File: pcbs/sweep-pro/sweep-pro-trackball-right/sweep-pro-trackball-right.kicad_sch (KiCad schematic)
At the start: 13 parts, among them J10 NFC Antenna, J3 Conn_01x07, J4 Conn_01x07, J5 Conn_01x02, J6 Conn_01x07, J7 Conn_01x03, J8 Conn_01x03, J9 Conn_Display_general

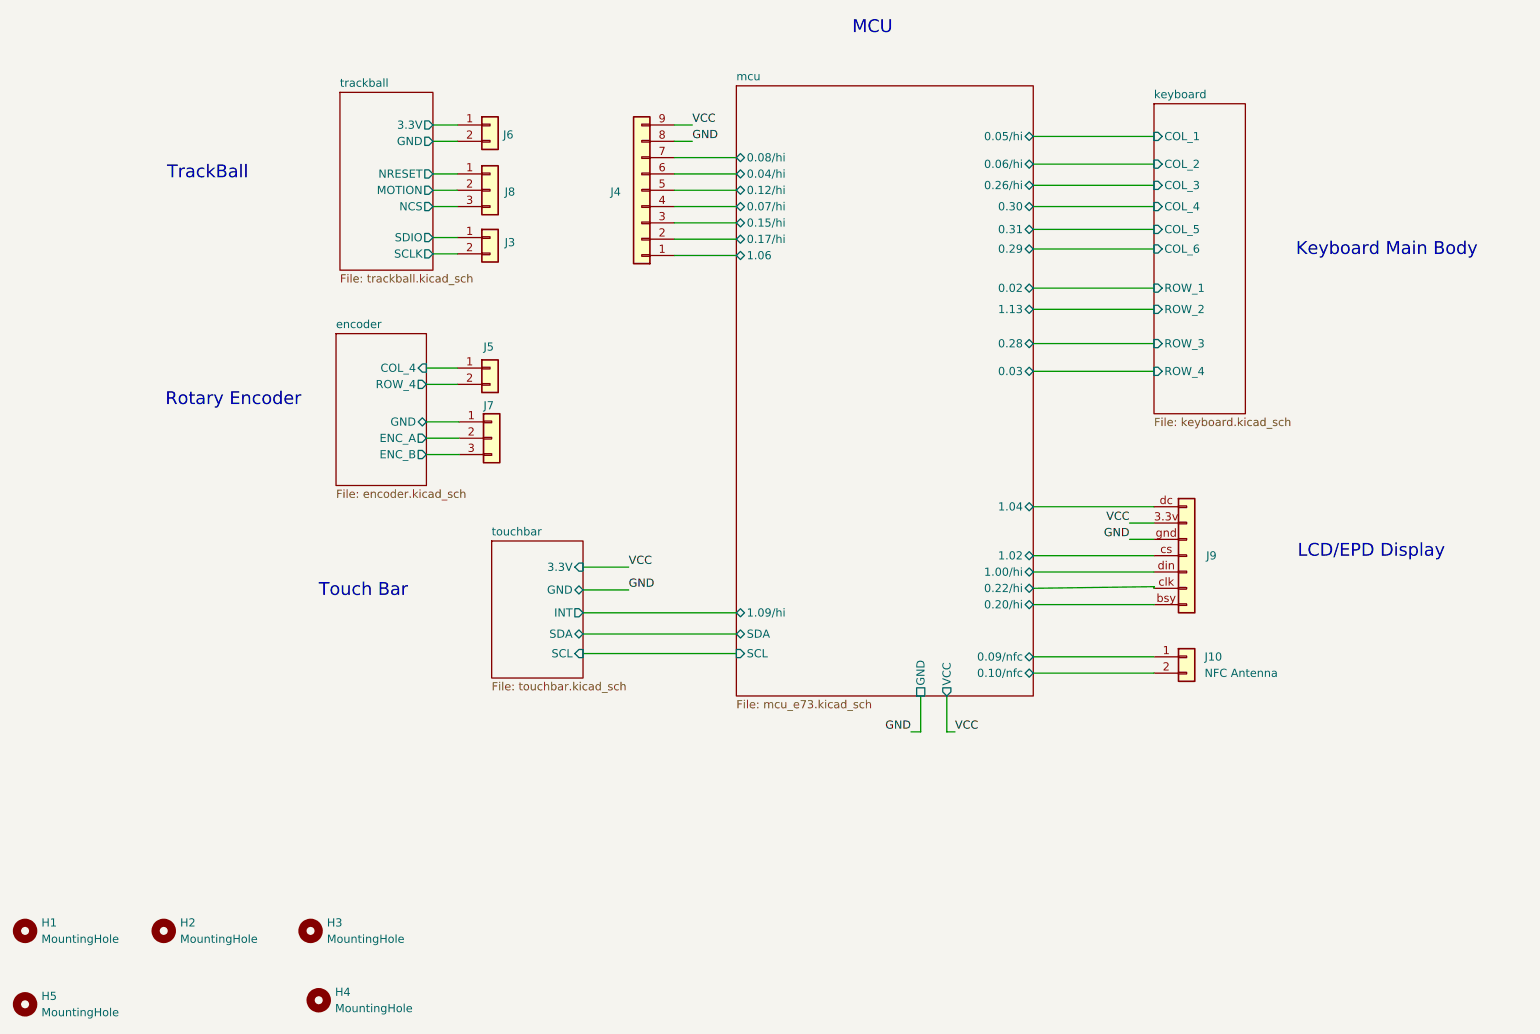
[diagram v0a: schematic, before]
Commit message: init version with integrated trackball in thumb position
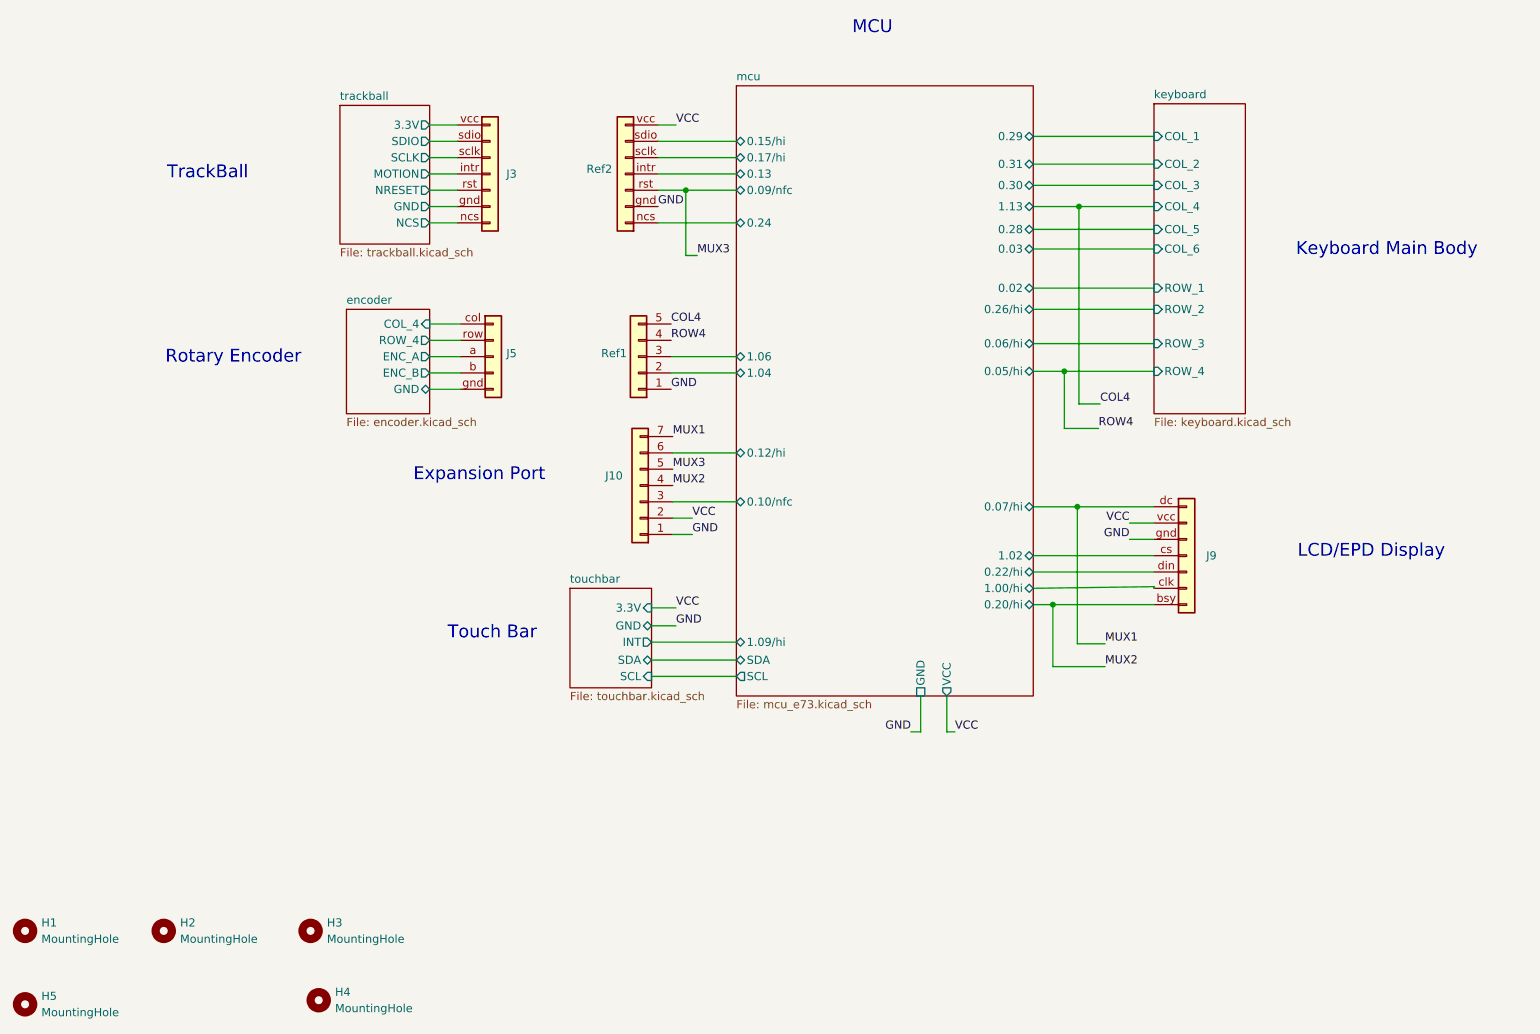
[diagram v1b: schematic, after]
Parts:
- removed J10: NFC Antenna, symbol Connector_Generic:Conn_01x02
- removed J3, J6: Conn_01x07, symbol Connector_Generic:Conn_01x02
- removed J7, J8: Conn_01x03, symbol Connector_Generic:Conn_01x03
- added J10: Conn_01x07, mylib:Magnetic-PogoPin-1x07-Male, symbol Connector_Generic:Conn_01x07
- added J3: Conn_01x07, mylib:PMW3610-Ref-Male, symbol Connector_Generic:Conn_01x07
- added Ref1: Conn_01x05, mylib:Panasonic_EVQWGD001_Ref, symbol Connector_Generic:Conn_01x05
- J5: value Conn_01x02 -> Conn_01x05; footprint (none) -> mylib:Panasonic_EVQWGD001_Ref_Male; symbol Connector_Generic:Conn_01x02 -> Connector_Generic:Conn_01x05; now left out of the parts list
- J9: footprint mylib:Conn_LCD -> mylib:Conn_Display_MountHole
- Ref2: renamed from J4; value Conn_01x07 -> Conn_1x07; footprint (none) -> mylib:PMW3610-Ref; symbol Connector_Generic:Conn_01x09 -> Connector_Generic:Conn_01x07; now left out of the parts list
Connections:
- net GND: now also Ref2.gnd, J10.1 (Pin_1), Ref1.1 (Pin_1); no longer Ref2.8 (Pin_8)
- net VCC: now also J9.vcc, Ref2.vcc, J10.2 (Pin_2); no longer J9.3.3v, Ref2.9 (Pin_9)
- net encoder/COL_4: now also J5.col; no longer J5.1 (Pin_1)
- net encoder/ENC_A: now also J5.a
- net encoder/ENC_B: now also J5.b
- net encoder/GND: now also J5.gnd
- net encoder/ROW_4: now also J5.row; no longer J5.2 (Pin_2)
- net mcu/0.10/nfc: now also J10.3 (Pin_3)
- net mcu/0.12/hi: now also J10.6 (Pin_6); no longer Ref2.5 (Pin_5)
- net mcu/0.15/hi: now also Ref2.sdio; no longer Ref2.3 (Pin_3)
- net mcu/0.17/hi: now also Ref2.sclk; no longer Ref2.2 (Pin_2)
- net mcu/0.22/hi: now also J9.din; no longer J9.clk
- net mcu/1.00/hi: now also J9.clk; no longer J9.din
- net mcu/1.04: now also Ref1.2 (Pin_2); no longer J9.dc
- net mcu/1.06: now also Ref1.3 (Pin_3); no longer Ref2.1 (Pin_1)
- net trackball/3.3V: now also J3.vcc
- net trackball/GND: now also J3.gnd
- net trackball/MOTION: now also J3.intr (motion)
- net trackball/NCS: now also J3.ncs
- net trackball/NRESET: now also J3.rst
- net trackball/SCLK: now also J3.sclk
- net trackball/SDIO: now also J3.sdio
- removed net mcu/0.04/hi: Ref2.6 (Pin_6)
- removed net mcu/0.07/hi: Ref2.4 (Pin_4)
- removed net mcu/0.08/hi: Ref2.7 (Pin_7)
- net mcu/0.20/hi renamed MUX2
- net MUX2: now also J10.4 (Pin_4)
- new net COL4: Ref1.5 (Pin_5)
- new net MUX1: J10.7 (Pin_7), J9.dc
- new net MUX3: J10.5 (Pin_5), Ref2.rst
- new net ROW4: Ref1.4 (Pin_4)
- new net mcu/0.13: Ref2.intr (motion)
- new net mcu/0.24: Ref2.ncs
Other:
- sheet mcu ports: added 0.13, 0.24; removed 0.04/hi, 0.08/hi
- note added: "Expansion Port"
